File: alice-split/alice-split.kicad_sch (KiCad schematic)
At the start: 88 parts, among them J1 MJ-4PP-9-Lily58-cache-Lily58_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, J2 OLED-Lily58-cache, U1 Sparkfun_Pro_Micro

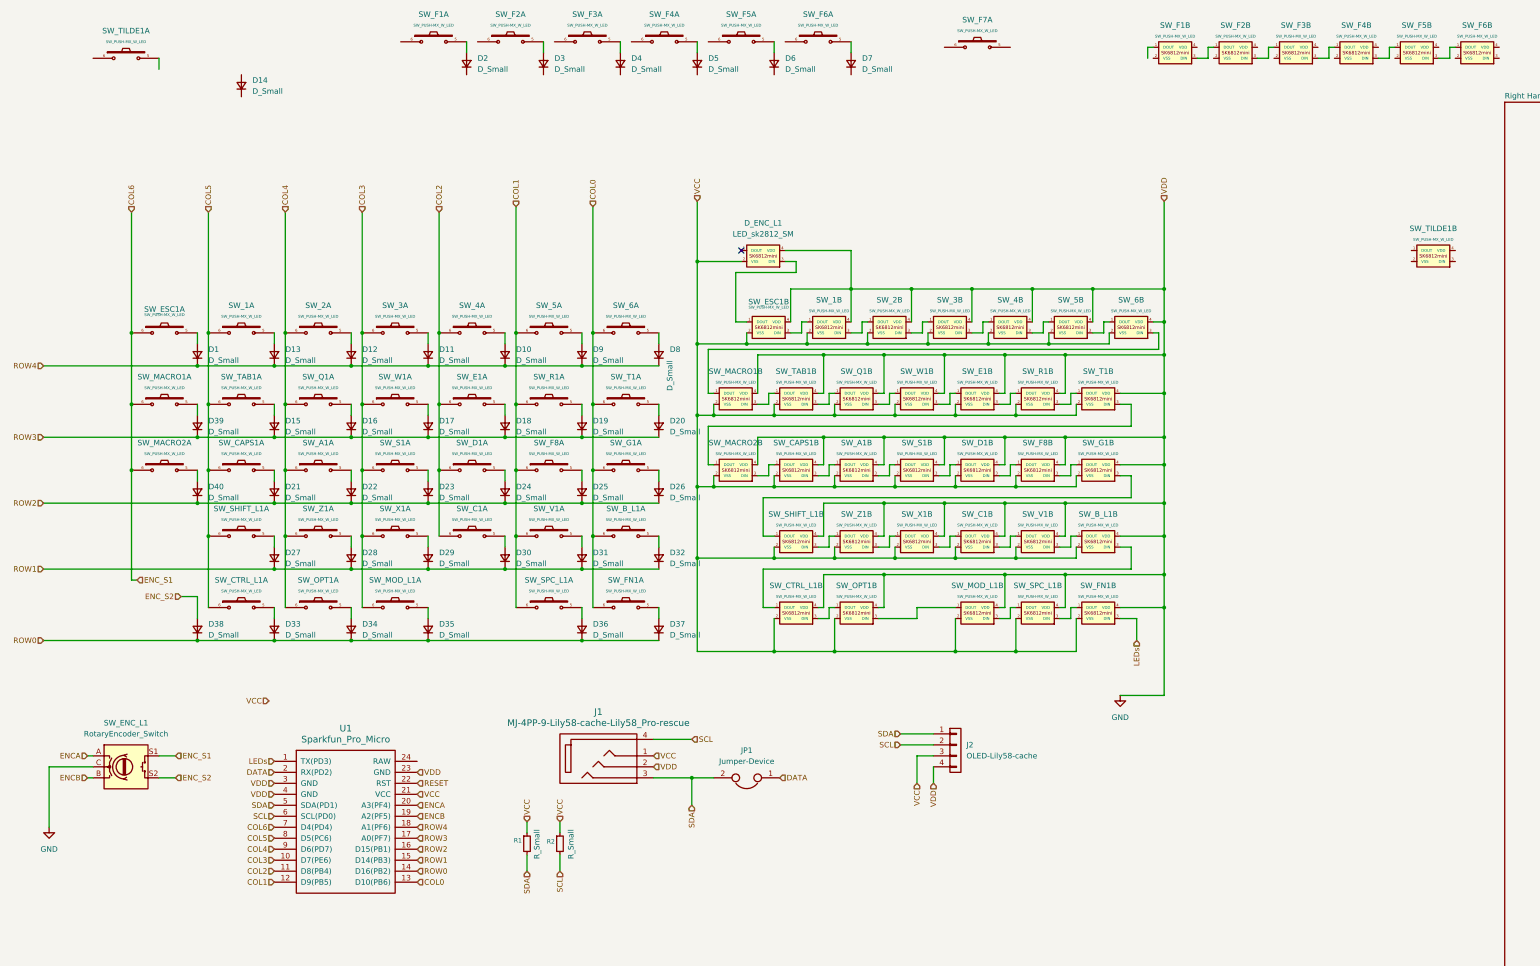
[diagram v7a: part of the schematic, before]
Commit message: Rewired Left Hand Side and Edge Cuts
Rewired the entire left hand side of the keyboard. Also added the edge cuts for the outer shape of each board. Redid this part on the left hand side to make it match the design of the right hand side.
Will start working on the rewiring of the right hand side next.
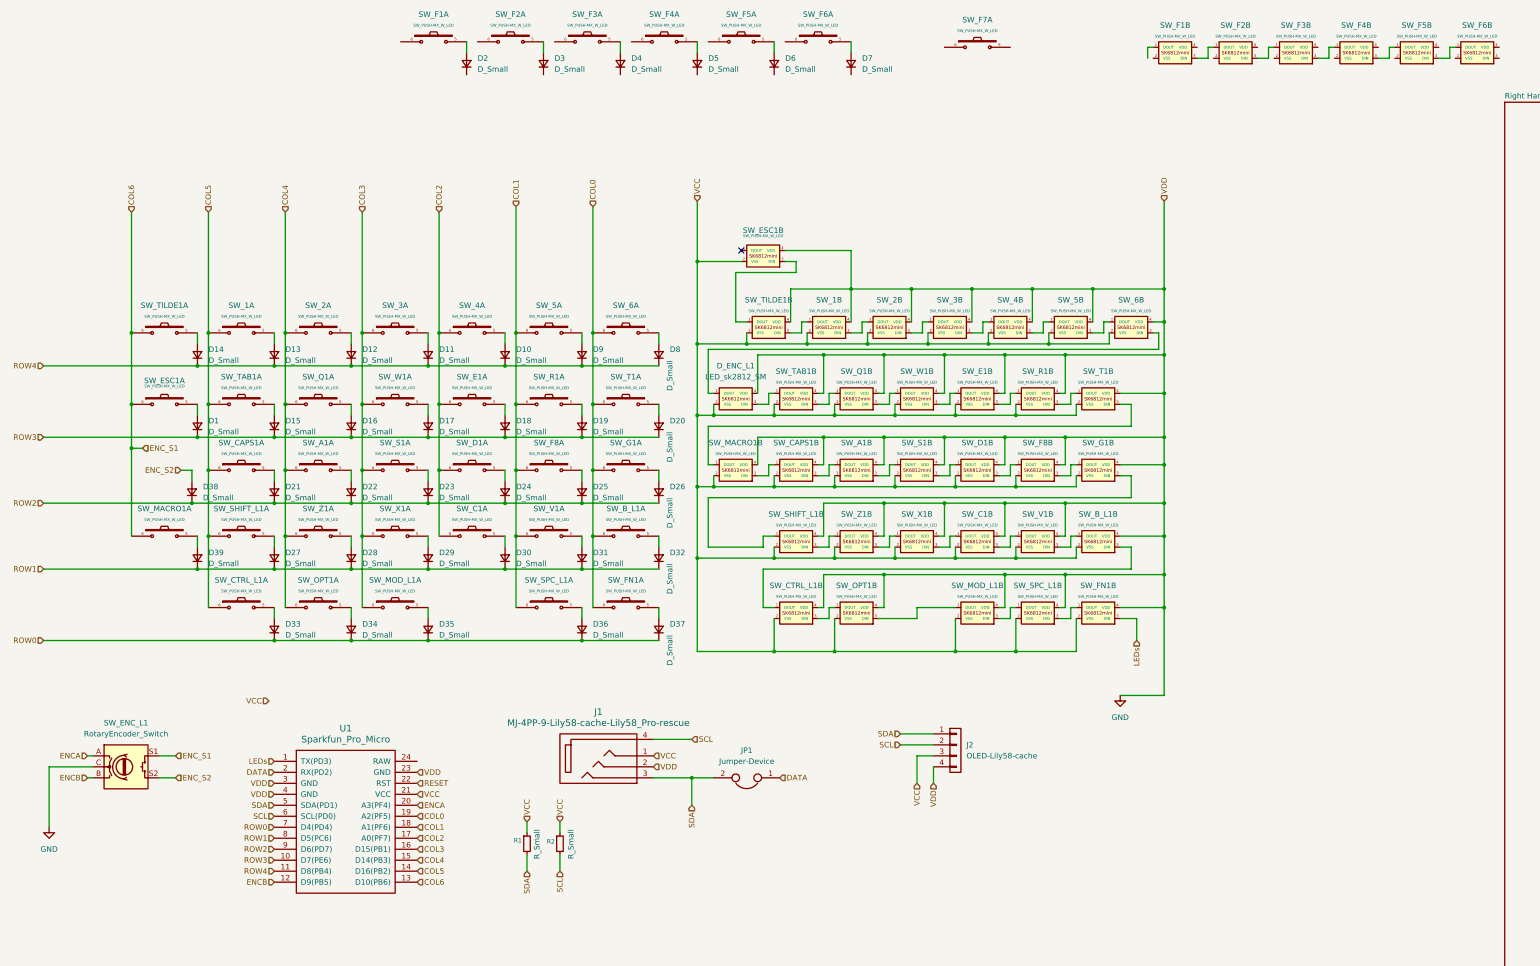
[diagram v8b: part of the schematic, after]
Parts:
- removed D40: D_Small, Diode_SMD:D_1206_3216Metric, symbol Device:D_Small
- removed SW_MACRO2: SW_PUSH-MX_W_LED, SofleRGB:SK6812MINI_and_cherry, symbol SofleKeyboard:SW_PUSH-MX_W_LED
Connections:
- net COL0: now also U1.19 (A2(PF5)); no longer U1.13 (D10(PB6))
- net COL1: now also U1.18 (A1(PF6)); no longer U1.12 (D9(PB5))
- net COL2: now also U1.17 (A0(PF7)); no longer U1.11 (D8(PB4))
- net COL3: now also U1.16 (D15(PB1)); no longer U1.10 (D7(PE6))
- net COL4: now also U1.15 (D14(PB3)); no longer U1.9 (D6(PD7))
- net COL5: now also U1.14 (D16(PB2)); no longer U1.8 (D5(PC6))
- net COL6: now also SW_TILDE1.6, U1.13 (D10(PB6)); no longer U1.7 (D4(PD4))
- net ENCB: now also U1.12 (D9(PB5)); no longer U1.19 (A2(PF5))
- net GND: now also SW_TILDE1.4 (VDD)
- net ROW0: now also U1.7 (D4(PD4)); no longer D38.1 (K), U1.14 (D16(PB2))
- net ROW1: now also D39.1 (K), U1.8 (D5(PC6)); no longer U1.15 (D14(PB3))
- net ROW2: now also D38.1 (K), U1.9 (D6(PD7)); no longer U1.16 (D15(PB1))
- net ROW3: now also D1.1 (K), U1.10 (D7(PE6)); no longer D39.1 (K), U1.17 (A0(PF7))
- net ROW4: now also D14.1 (K), U1.11 (D8(PB4)); no longer D1.1 (K), U1.18 (A1(PF6))
- net VCC: now also SW_TILDE1.2 (VSS)
- net at SW_MACRO1.1 (DOUT): now also SW_T1.3 (DIN); no longer SW_6.3 (DIN)
- net at SW_MACRO1.3 (DIN): now also SW_CAPS1.1 (DOUT); no longer SW_TAB1.1 (DOUT)
- net at SW_1.1 (DOUT): now also SW_TILDE1.3 (DIN); no longer SW_ESC1.3 (DIN)
- net at D_ENC_L1.1 (DOUT): now also SW_6.3 (DIN)
- net at D_ENC_L1.3 (DIN): now also SW_TAB1.1 (DOUT); no longer SW_ESC1.1 (DOUT)
- net at SW_TILDE1.1 (DOUT): now also SW_ESC1.3 (DIN)
- net at D14.2 (A): now also SW_TILDE1.5
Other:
- moved on the sheet: D1, D14, D38, D39, D_ENC_L1, SW_ESC1A, SW_ESC1B, SW_MACRO1A, SW_MACRO1B, SW_TILDE1A, SW_TILDE1B
